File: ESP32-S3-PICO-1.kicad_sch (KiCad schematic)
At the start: 17 parts, among them CN3 2337019-1, U1 SKYA21024, U6 ESP32-S3-PICO-1-N8R2, U9 TS3USB221A-Q1

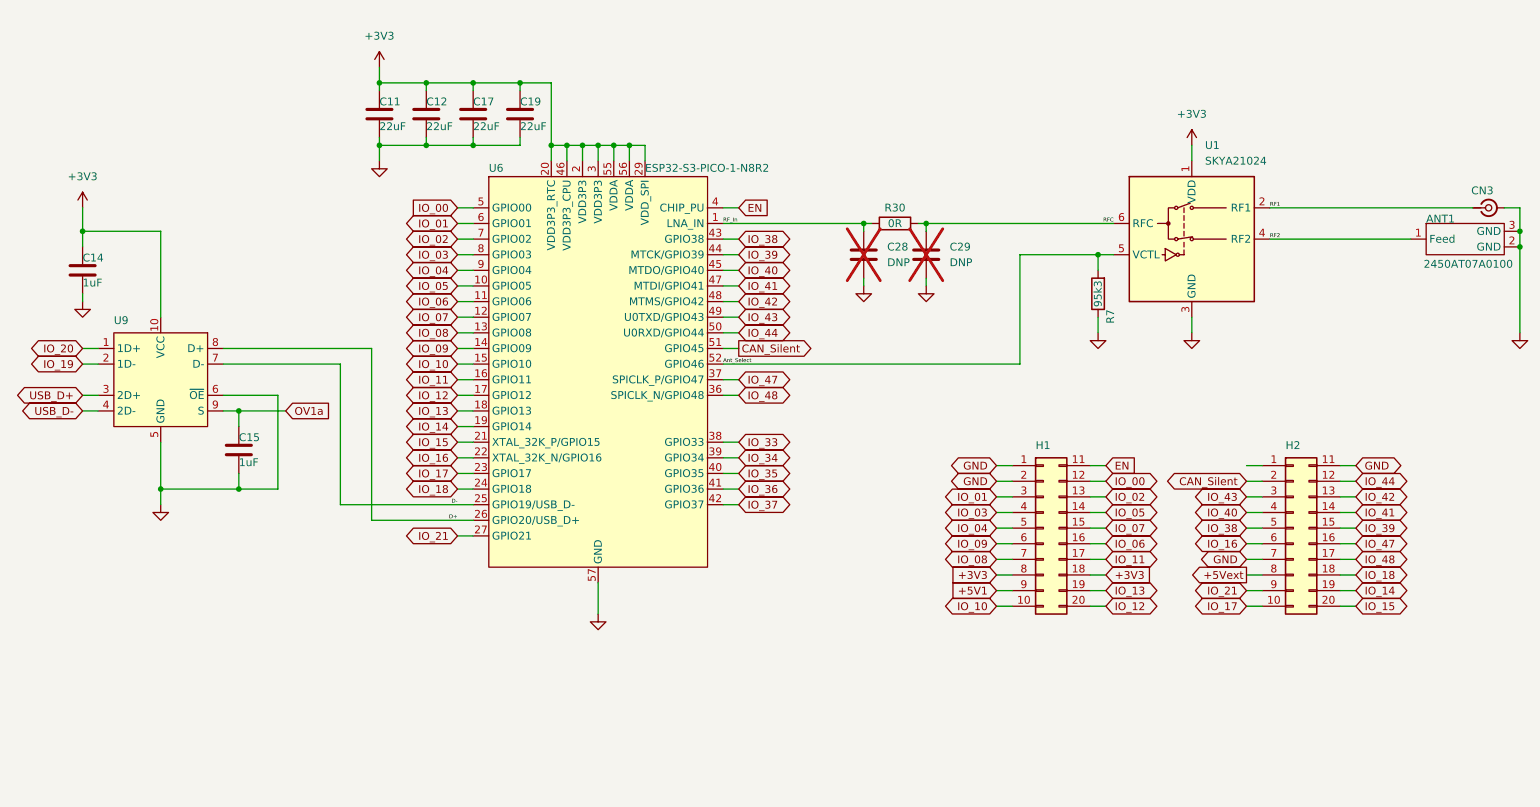
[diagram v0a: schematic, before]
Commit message: streamlined routing by discarding legacy GPIO pinout compatibility. reduced Vin to Vcc and Vbus (no more +16V) includes CAN & Vehicle inputs (need to move to 2nd board, though) added wake-on-start by wiring Vacc to RTC_IO
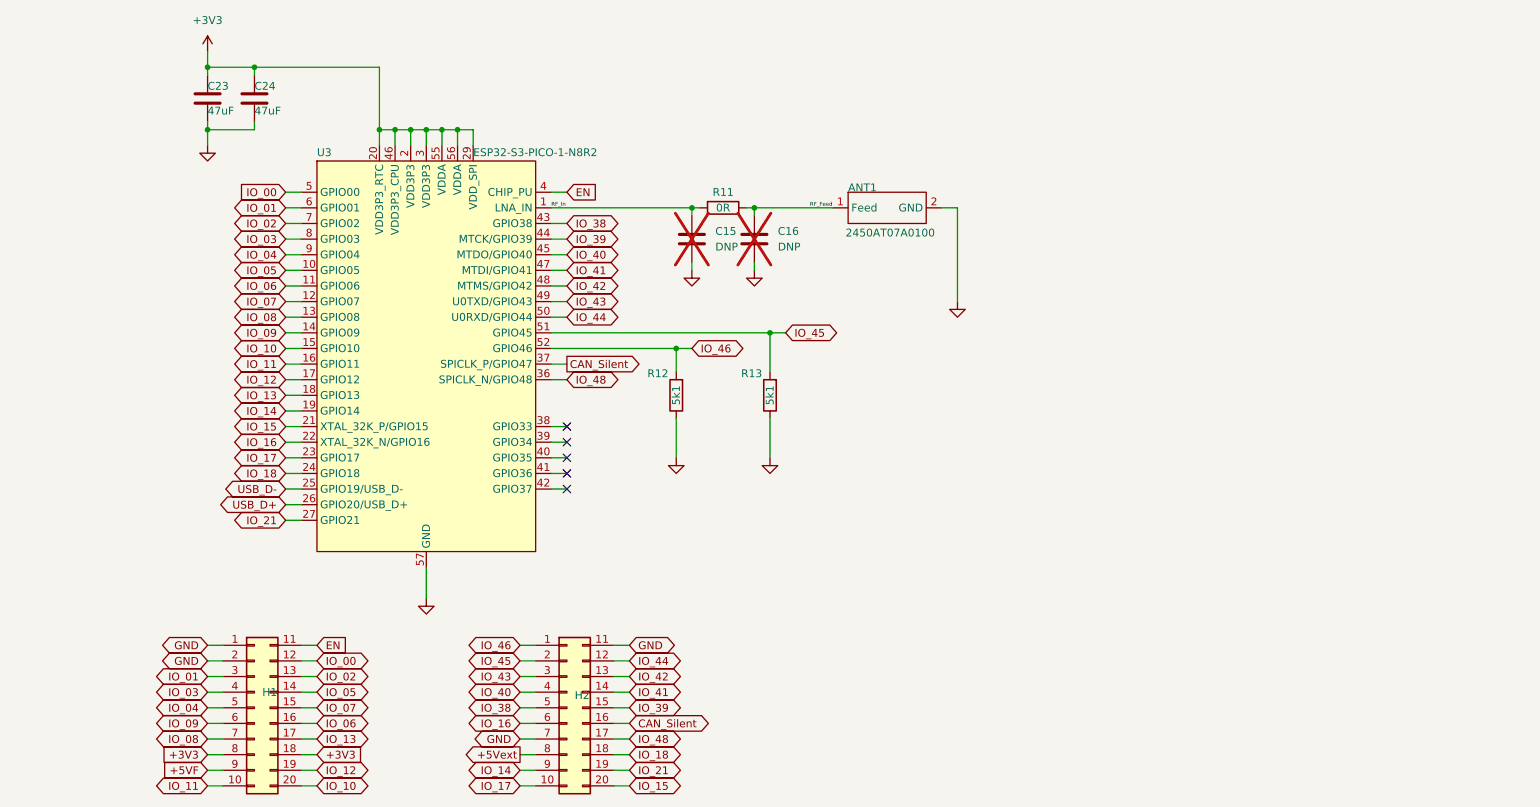
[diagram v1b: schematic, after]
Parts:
- removed C11, C12, C17, C19: 22uF, Capacitors:C0402_Dense, symbol Device:C
- removed C14, C15: 1uF, Capacitors:C0201_Dense, symbol Device:C
- removed CN3: 2337019-1, Personal_FootprintLibrary:u.FL_Male_Pin_Coax_SMD, symbol Connector:Conn_Coaxial_Small
- removed R7: 95k3, Resistors:R0201_Dense, symbol Device:R
- removed U1: SKYA21024, Personal_FootprintLibrary:SKYA21024, symbol PersonalSchematicSymbolLibrary:SKYA21024
- removed U9: TS3USB221A-Q1, Personal_FootprintLibrary:Texas_UQFN-10_1.5x2mm_P0.5mm, symbol PersonalSchematicSymbolLibrary:TS3USB221A-Q1
- added C23, C24: 47uF, Capacitors:C_0603_Dense, symbol Device:C
- added R12, R13: 5k1, Resistors:R_0201_Dense, symbol Device:R
- ANT1: FT Origin (none) -> Anchor
- C15: renamed from C28; footprint Capacitors:C0201_Dense -> Capacitors:C_0201_Dense
- C16: renamed from C29; footprint Capacitors:C0201_Dense -> Capacitors:C_0201_Dense
- H1, H2: footprint Personal_FootprintLibrary:PinHeader_2x10_P2.54mm_Vertical -> Personal_FootprintLibrary:PinHeader_2x10_P2.54mm_Vertical_BottomMount_TopReference
- R11: renamed from R30; footprint Resistors:R0201_Dense -> Resistors:R_0201_Dense
- renumbered U6 to U3
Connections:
- net Ant_Select is gone; now on net IO_46: U3.52 (GPIO46)
- net D+ is gone; now on net USB_D+: U3.26 (GPIO20/USB_D+)
- net D- is gone; now on net USB_D-: U3.25 (GPIO19/USB_D-)
- net IO_47 is gone; now on net CAN_Silent: H2.16 (Pin_16), U3.37 (SPICLK_P/GPIO47)
- net RFC is gone; now on net RF_Feed: C16.1, R11.2
- net +3V3: now also C23.1, C24.1
- net CAN_Silent: no longer H2.2 (Pin_2), U3.51 (GPIO45)
- net GND: now also C23.2, C24.2, R12.1, R13.1
- net IO_10: now also H1.20 (Pin_20); no longer H1.10 (Pin_10)
- net IO_11: now also H1.10 (Pin_10); no longer H1.17 (Pin_17)
- net IO_12: now also H1.19 (Pin_19); no longer H1.20 (Pin_20)
- net IO_13: now also H1.17 (Pin_17); no longer H1.19 (Pin_19)
- net IO_14: now also H2.9 (Pin_9); no longer H2.19 (Pin_19)
- net IO_21: now also H2.19 (Pin_19); no longer H2.9 (Pin_9)
- net IO_46: now reaches H2.1 (Pin_1)
- net IO_46: now also R12.2
- net +5V1 renamed +5VF
- net IO_33: no longer names the net of U3.38 (GPIO33)
- net IO_34: no longer names the net of U3.39 (GPIO34)
- net IO_35: no longer names the net of U3.40 (GPIO35)
- net IO_36: no longer names the net of U3.41 (GPIO36)
- net IO_37: no longer names the net of U3.42 (GPIO37)
- net RF2 renamed RF_Feed
- new net IO_45: H2.2 (Pin_2), R13.2, U3.51 (GPIO45)
- no-connect marks 0 -> 5
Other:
- moved on the sheet: C15, C16, H1, H2, R11, U3

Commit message: Update .gitignore, BOM-ESP32-S3 Pico D1.csv, CANBus_Interface.kicad_sch, and 14 more files
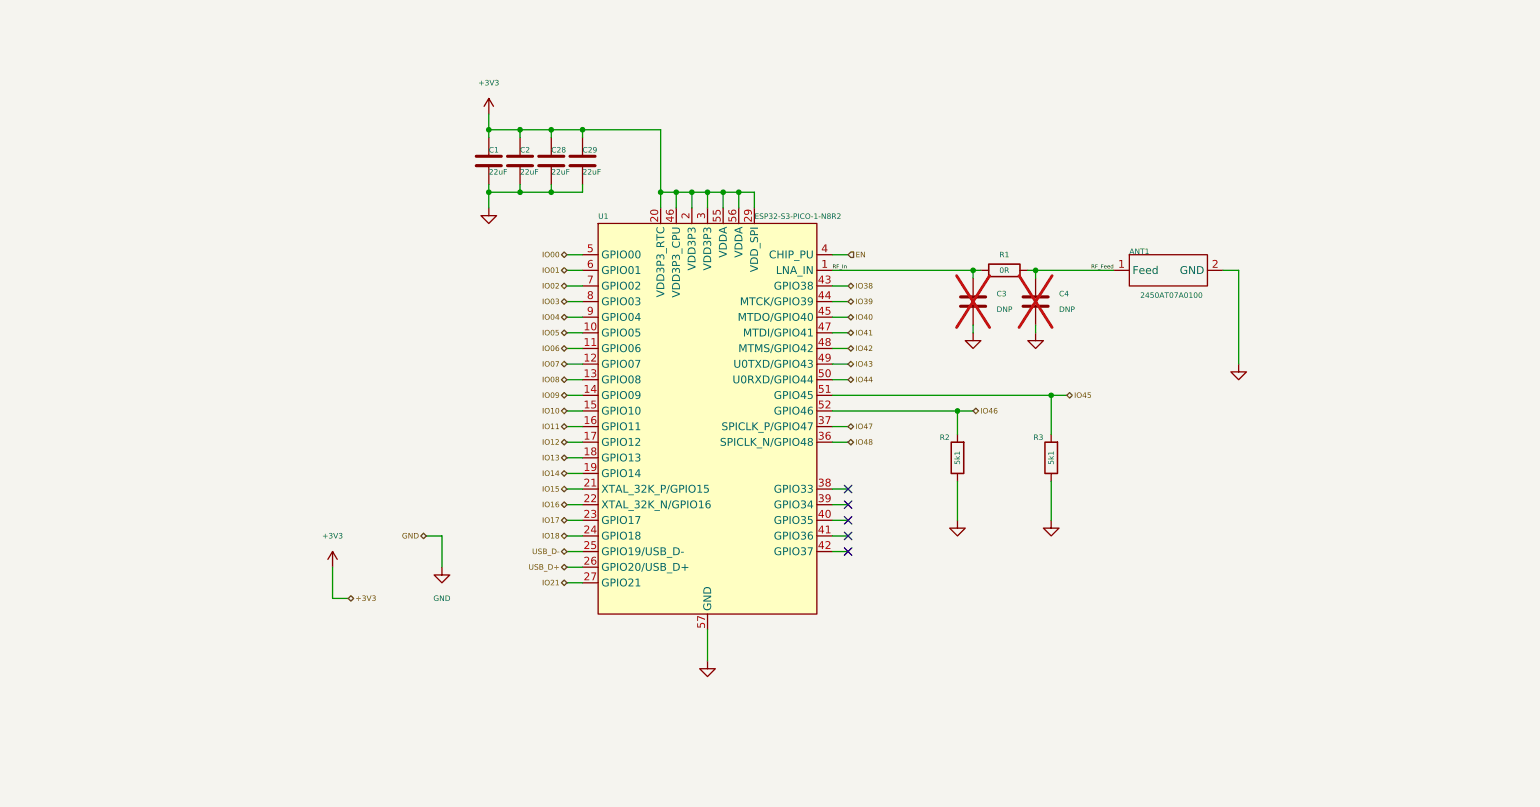
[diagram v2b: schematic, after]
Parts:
- removed C24: 47uF, Capacitors:C_0603_Dense, symbol Device:C
- removed H1, H2: ESP_Header, Personal_FootprintLibrary:PinHeader_2x10_P2.54mm_Vertical_BottomMount_TopReference, symbol PersonalSchematicSymbolLibrary:Conn_02x10_Top_Bottom_MountingPin
- removed R12, R13: 5k1, Resistors:R_0201_Dense, symbol Device:R
- added C2, C28, C29: 22uF, Capacitors:C_0603_Dense, symbol Device:C
- added R2, R3: 5k1, Resistors:R_0201_Dense, symbol Device:R
- C1: renamed from C23; value 47uF -> 22uF; Distributor Link 1 https://www.digikey.com/en/products/detail/murata-electroni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 -> https://www.digikey.com/en/products/detail/samsung-electro-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; Distributor Link 2 https://www.mouser.com/ProductDetail/Murata-Electronics/GRM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 -> https://www.mouser.com/ProductDetail/Samsung-Electro-Mechan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; LCSC C140782 -> C2762594; Manufacturer Murata Electronics -> Samsung Electro-Mechanics; Manufacturer Part Number GRM188R60J476ME15D -> CL10A226MO7JZNC
- renumbered C15 to C3, C16 to C4, R11 to R1, U3 to U1
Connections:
- net +3V3: now also C2.1, C28.1, C29.1
- net GND: now also C2.2, C28.2, C29.2, R2.1, R3.1
- net CAN_Silent renamed IO47
- net IO_00 renamed IO00
- net IO_01 renamed IO01
- net IO_02 renamed IO02
- net IO_03 renamed IO03
- net IO_04 renamed IO04
- net IO_05 renamed IO05
- net IO_06 renamed IO06
- net IO_07 renamed IO07
- net IO_08 renamed IO08
- net IO_09 renamed IO09
- net IO_10 renamed IO10
- net IO_11 renamed IO11
- net IO_12 renamed IO12
- net IO_13 renamed IO13
- net IO_14 renamed IO14
- net IO_15 renamed IO15
- net IO_16 renamed IO16
- net IO_17 renamed IO17
- net IO_18 renamed IO18
- net IO_21 renamed IO21
- net IO_38 renamed IO38
- net IO_39 renamed IO39
- net IO_40 renamed IO40
- net IO_41 renamed IO41
- net IO_42 renamed IO42
- net IO_43 renamed IO43
- net IO_44 renamed IO44
- net IO_45 renamed IO45
- net IO45: now also R3.2
- net IO_46 renamed IO46
- net IO46: now also R2.2
- net IO_48 renamed IO48
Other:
- moved on the sheet: ANT1, C1, C3, C4, R1, U1

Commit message: Update CANBus_Interface.kicad_sch, ESP32-S3 D1 Pico Board.kicad_sch, ESP32-S3 Pico D1.kicad_pcb, and 15 more files
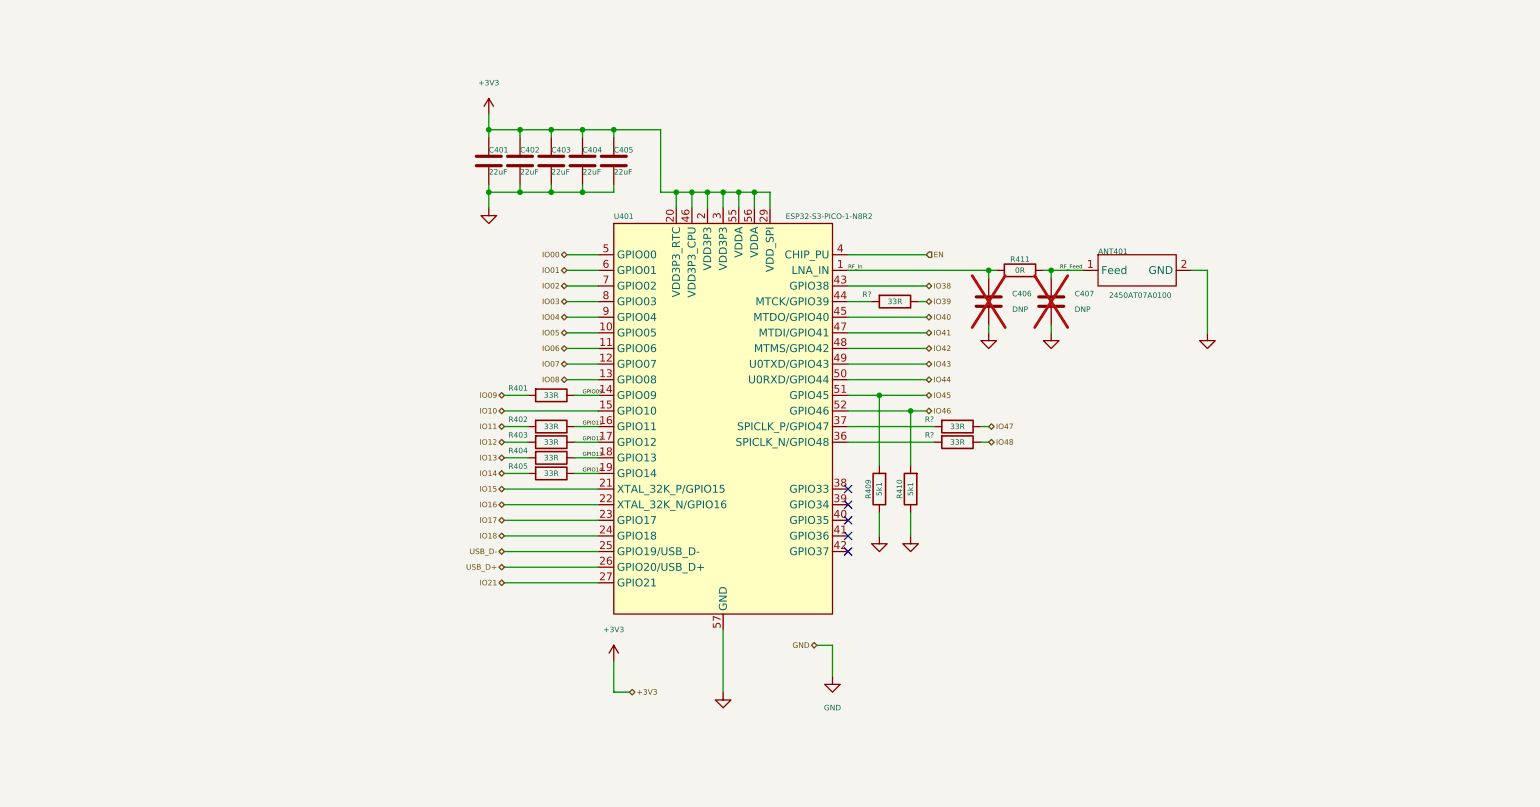
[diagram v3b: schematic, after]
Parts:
- added C405: 22uF, My Capacitors:C_0603_Dense, symbol Device:C
- added R401, R402, R403, R404, R405, R? (x3): 33R, My Resistors:R_0201_Dense, symbol Device:R
- C401: renamed from C1; footprint Capacitors:C_0603_Dense -> My Capacitors:C_0603_Dense; Distributor Link 1 https://www.digikey.com/en/products/detail/samsung-electro-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 -> https://www.digikey.com/en/products/detail/murata-electroni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; Distributor Link 2 https://www.mouser.com/ProductDetail/Samsung-Electro-Mechan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 -> https://www.mouser.com/ProductDetail/Murata-Electronics/GRM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; LCSC C2762594 -> C29519229; Manufacturer Samsung Electro-Mechanics -> Murata Electronics; Manufacturer Part Number CL10A226MO7JZNC -> GRM188C61E226ME01D
- C402: renamed from C2; footprint Capacitors:C_0603_Dense -> My Capacitors:C_0603_Dense; Distributor Link 1 https://www.digikey.com/en/products/detail/samsung-electro-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 -> https://www.digikey.com/en/products/detail/murata-electroni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; Distributor Link 2 https://www.mouser.com/ProductDetail/Samsung-Electro-Mechan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 -> https://www.mouser.com/ProductDetail/Murata-Electronics/GRM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; LCSC C2762594 -> C29519229; Manufacturer Samsung Electro-Mechanics -> Murata Electronics; Manufacturer Part Number CL10A226MO7JZNC -> GRM188C61E226ME01D
- C403: renamed from C28; footprint Capacitors:C_0603_Dense -> My Capacitors:C_0603_Dense; Distributor Link 1 https://www.digikey.com/en/products/detail/samsung-electro-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 -> https://www.digikey.com/en/products/detail/murata-electroni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; Distributor Link 2 https://www.mouser.com/ProductDetail/Samsung-Electro-Mechan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 -> https://www.mouser.com/ProductDetail/Murata-Electronics/GRM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; LCSC C2762594 -> C29519229; Manufacturer Samsung Electro-Mechanics -> Murata Electronics; Manufacturer Part Number CL10A226MO7JZNC -> GRM188C61E226ME01D
- C404: renamed from C29; footprint Capacitors:C_0603_Dense -> My Capacitors:C_0603_Dense; Distributor Link 1 https://www.digikey.com/en/products/detail/samsung-electro-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 -> https://www.digikey.com/en/products/detail/murata-electroni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; Distributor Link 2 https://www.mouser.com/ProductDetail/Samsung-Electro-Mechan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 -> https://www.mouser.com/ProductDetail/Murata-Electronics/GRM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; LCSC C2762594 -> C29519229; Manufacturer Samsung Electro-Mechanics -> Murata Electronics; Manufacturer Part Number CL10A226MO7JZNC -> GRM188C61E226ME01D
- C406: renamed from C3; footprint Capacitors:C_0201_Dense -> My Capacitors:C_0201_Dense
- C407: renamed from C4; footprint Capacitors:C_0201_Dense -> My Capacitors:C_0201_Dense
- R409: renamed from R2; footprint Resistors:R_0201_Dense -> My Resistors:R_0201_Dense
- R410: renamed from R3; footprint Resistors:R_0201_Dense -> My Resistors:R_0201_Dense
- R411: renamed from R1; footprint Resistors:R_0201_Dense -> My Resistors:R_0201_Dense; Distributor Link 1 https://www.digikey.com/en/products/detail/yageo/RC0201FR-0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 -> https://www.digikey.com/en/products/detail/yageo/AC0201JR-1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; Distributor Link 2 https://www.mouser.com/ProductDetail/YAGEO/RC0201FR-070RL?q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 -> https://www.mouser.com/ProductDetail/YAGEO/AC0201JR-130RL?q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; LCSC C106227 -> C6491732; Manufacturer Part Number RC0201FR-070RL -> AC0201JR-130RL
- renumbered ANT1 to ANT401, U1 to U401
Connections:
- net +3V3: now also C405.1
- net GND: now also C405.2
- net IO09: now also R401.2; no longer U401.14 (GPIO09)
- net IO11: now also R402.2; no longer U401.16 (GPIO11)
- net IO12: now also R403.2; no longer U401.17 (GPIO12)
- net IO13: now also R404.2; no longer U401.18 (GPIO13)
- net IO14: now also R405.2; no longer U401.19 (GPIO14)
- net IO39: now also R?.1; no longer U401.44 (MTCK/GPIO39)
- net IO45: now also R409.2; no longer R410.2
- net IO46: now also R410.2; no longer R409.2
- net IO47: now also R?.1; no longer U401.37 (SPICLK_P/GPIO47)
- net IO48: now also R?.1; no longer U401.36 (SPICLK_N/GPIO48)
- new net: R?.2, U401.44 (MTCK/GPIO39)
- new net: R?.2, U401.37 (SPICLK_P/GPIO47)
- new net: R?.2, U401.36 (SPICLK_N/GPIO48)
- new net GPIO09: R401.1, U401.14 (GPIO09)
- new net GPIO11: R402.1, U401.16 (GPIO11)
- new net GPIO12: R403.1, U401.17 (GPIO12)
- new net GPIO13: R404.1, U401.18 (GPIO13)
- new net GPIO14: R405.1, U401.19 (GPIO14)
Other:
- moved on the sheet: ANT401, C406, C407, R409, R410, R411, U401
